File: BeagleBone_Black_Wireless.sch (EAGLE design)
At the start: 274 parts, among them IC1 OSD3358, IC10 TXS0108ERGYR, IC11 TXS0108ERGYR, IC12 TPS2051BDGN, IC13 SN74AUC1G74, IC14 TPD4S012DRY, IC15 TPD4S012DRY, IC17 SN74LVC2G241DCUR, IC18 TL1963ADCQR, IC19 AP2112K-1.8TRG1 3.3V, IC2 SN74LVC1G07DCK, IC3 SN74LVC1G06DCK, IC4 24LC32AT-I/OT, IC5 TLVH431 (SOT-23-3), IC6 DNP TLVH431 (SOT-23-3), IC7 IP4283CZ10-TBR, IC8 IP4283CZ10-TBR, Q2 32.768kHz, Q4 24 MHz, T1 MMBT2907, T2 DNP MMBT2907, T3 BSS138W-7-F, T4 BSS138W-7-F, X2 SCHA5B0200, X4 10118192-0001LF, X5 10118241-001RLF

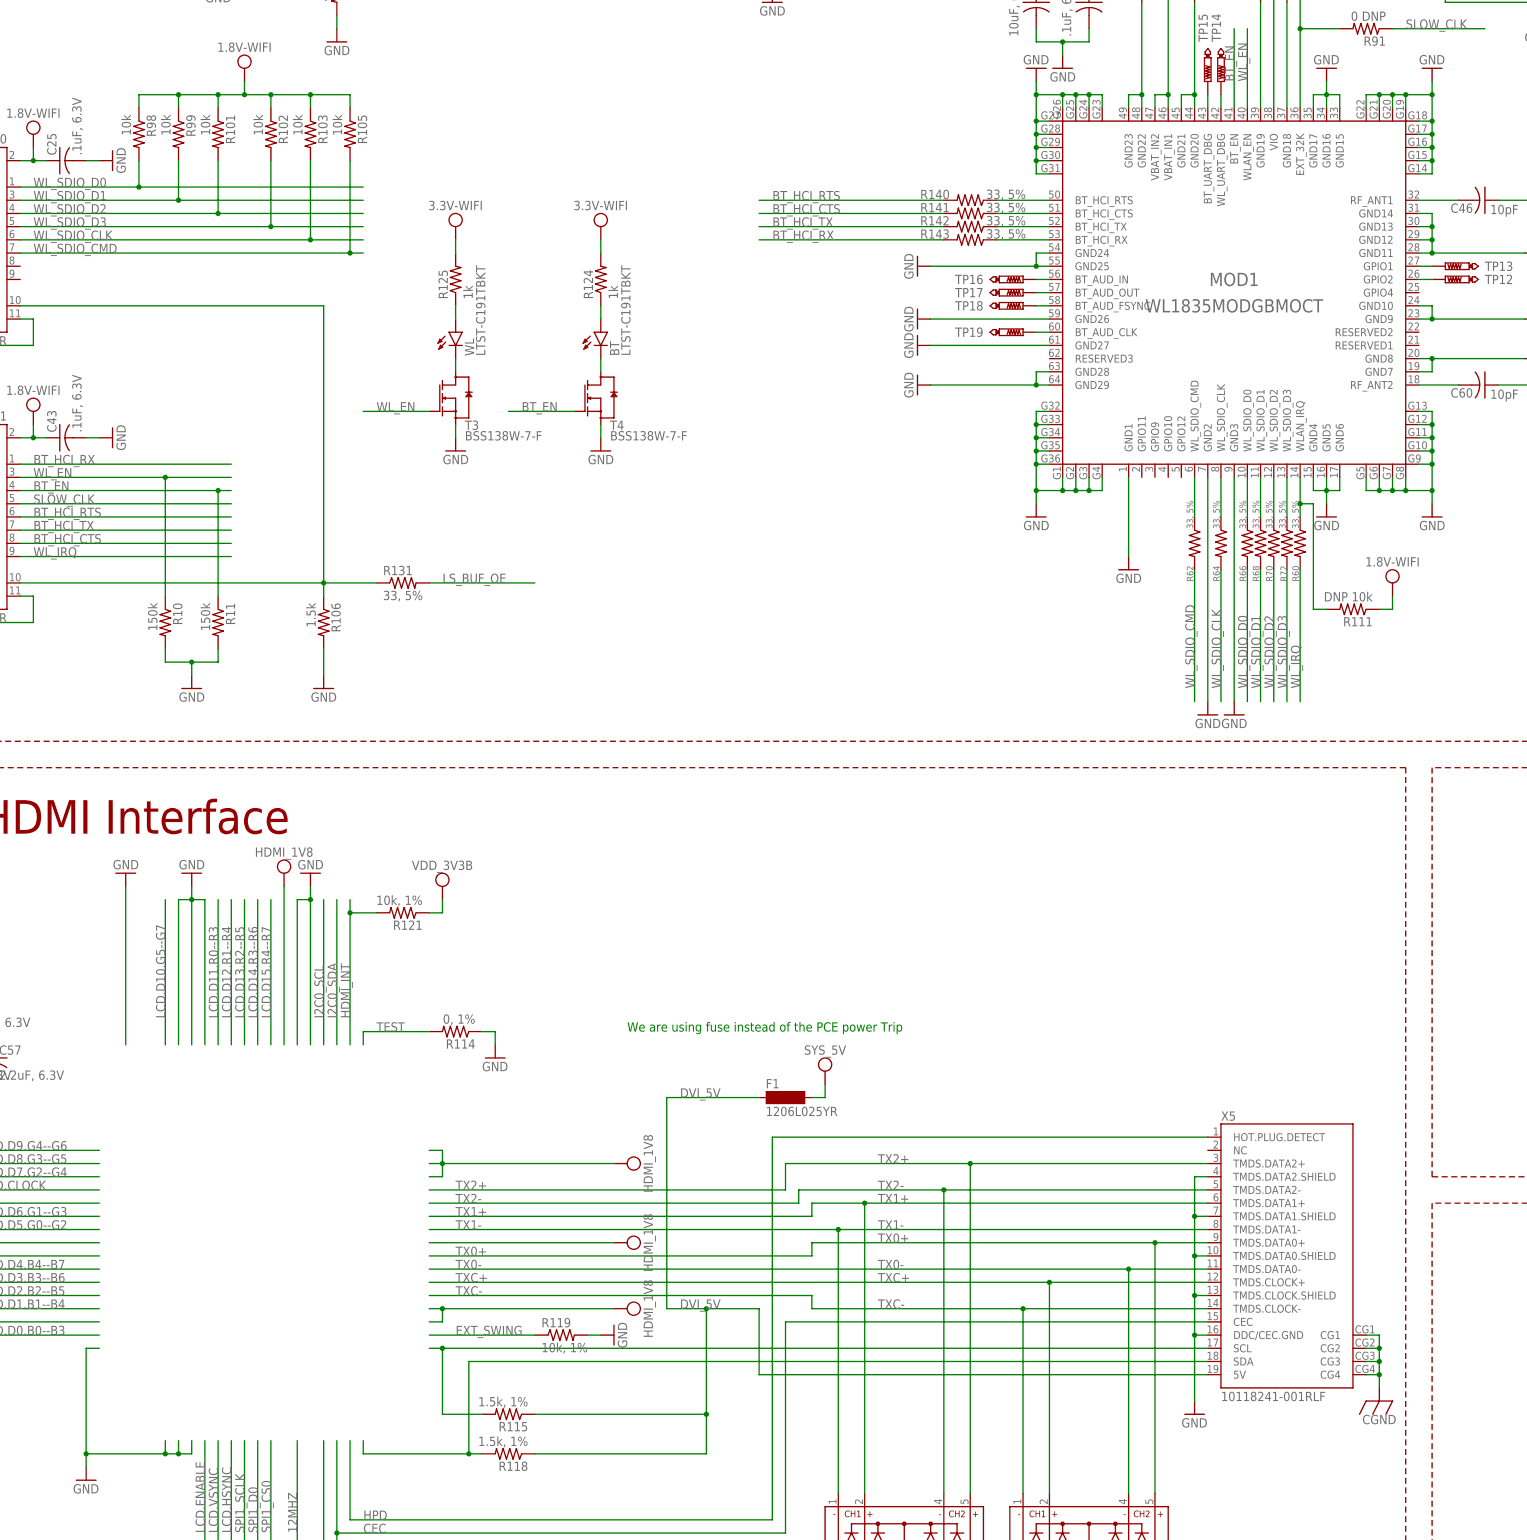
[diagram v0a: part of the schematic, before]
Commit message: removed MOD1 - added IC9 - adjusted routes
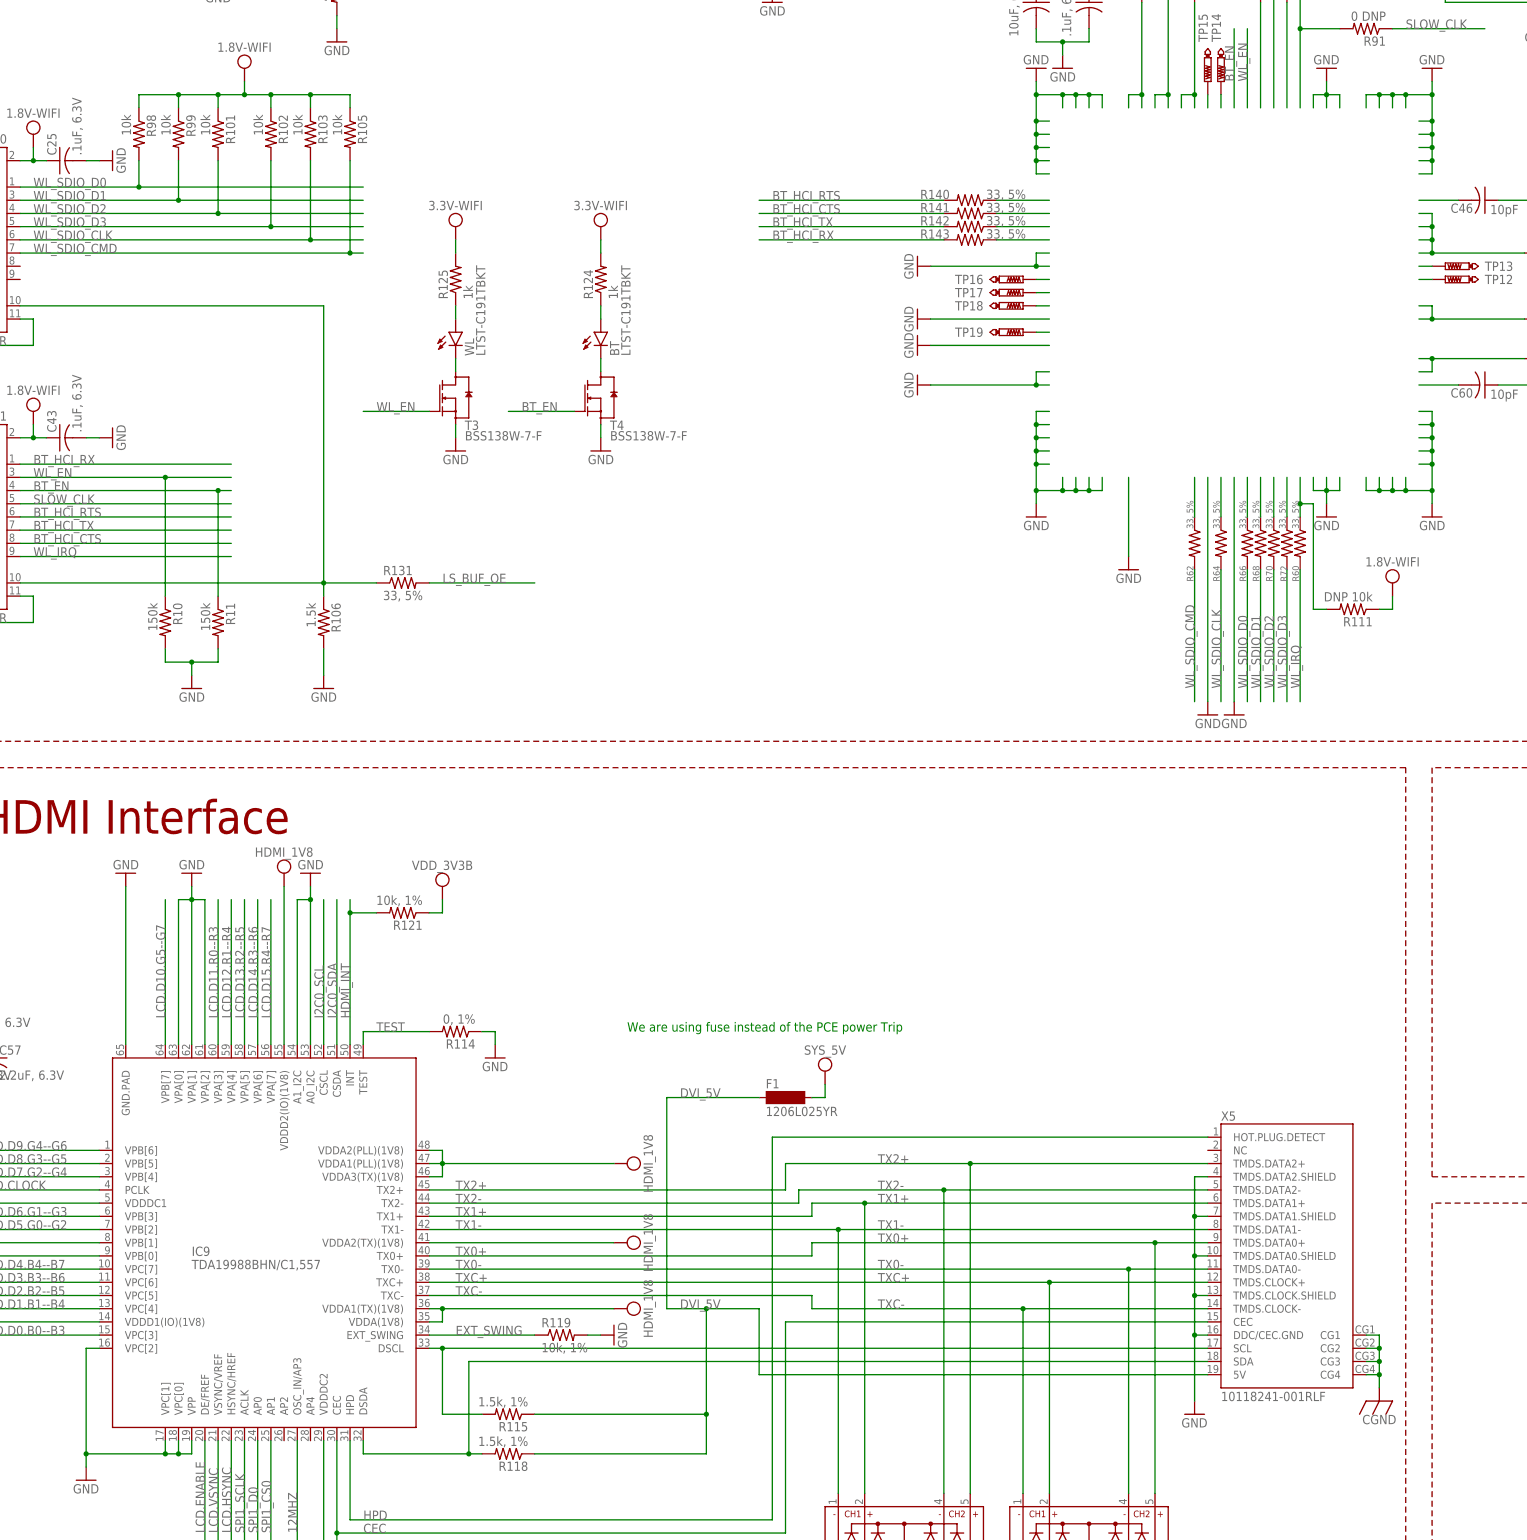
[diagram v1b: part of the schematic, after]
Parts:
- removed MOD1: WL1835MODGBMOCT, GHI-IC:WL1835MOD
- added IC9: TDA19988BHN/C1,557, GHI-IC:TDA19988BHN/C1
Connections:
- net 1.8V-WIFI: no longer MOD1.VIO
- net 12MHZ: now also IC9.OSC_IN/AP3
- net 3.3V-WIFI: no longer MOD1.VBAT_IN1, MOD1.VBAT_IN2
- net 32.768KHZ: no longer MOD1.EXT_32K
- net BT_EN: no longer MOD1.BT_EN
- net CEC: now also IC9.CEC
- net EXT_SWING: now also IC9.EXT_SWING
- net GND: now also IC9.A0_I2C, IC9.A1_I2C, IC9.GND.PAD, IC9.VPA[0], IC9.VPA[1], IC9.VPA[2], IC9.VPB[0], IC9.VPB[1], IC9.VPC[0], IC9.VPC[1], IC9.VPC[2], IC9.VPP; no longer MOD1.G1, MOD1.G10, MOD1.G11, MOD1.G12, MOD1.G13, MOD1.G14, MOD1.G15, MOD1.G16, MOD1.G17, MOD1.G18, MOD1.G19, MOD1.G2, MOD1.G20, MOD1.G21, MOD1.G22, MOD1.G23, MOD1.G24, MOD1.G25, MOD1.G26, MOD1.G27, MOD1.G28, MOD1.G29, MOD1.G3, MOD1.G30, MOD1.G31, MOD1.G32, MOD1.G33, MOD1.G34, MOD1.G35, MOD1.G36, MOD1.G4, MOD1.G5, MOD1.G6, MOD1.G7, MOD1.G8, MOD1.G9, MOD1.GND1, MOD1.GND10, MOD1.GND11, MOD1.GND12, MOD1.GND13, MOD1.GND14, MOD1.GND15, MOD1.GND16, MOD1.GND17, MOD1.GND18, MOD1.GND19, MOD1.GND2, MOD1.GND20, MOD1.GND21, MOD1.GND22, MOD1.GND23, MOD1.GND24, MOD1.GND25, MOD1.GND26, MOD1.GND27, MOD1.GND28, MOD1.GND29, MOD1.GND3, MOD1.GND4, MOD1.GND5, MOD1.GND6, MOD1.GND7, MOD1.GND8, MOD1.GND9
- net HDMI.DSCL: now also IC9.DSCL
- net HDMI.DSDA: now also IC9.DSDA
- net HDMI_1V8: now also IC9.VDDA(1V8), IC9.VDDA1(PLL)(1V8), IC9.VDDA1(TX)(1V8), IC9.VDDA2(PLL)(1V8), IC9.VDDA2(TX)(1V8), IC9.VDDA3(TX)(1V8), IC9.VDDD1(IO)(1V8), IC9.VDDD2(IO)(1V8), IC9.VDDDC1, IC9.VDDDC2
- net HDMI_INT: now also IC9.INT
- net HPD: now also IC9.HPD
- net I2C0_SCL: now also IC9.CSCL
- net I2C0_SDA: now also IC9.CSDA
- net LCD.CLOCK: now also IC9.PCLK
- net LCD.D0.B0--B3: now also IC9.VPC[3]
- net LCD.D1.B1--B4: now also IC9.VPC[4]
- net LCD.D10.G5--G7: now also IC9.VPB[7]
- net LCD.D11.R0--R3: now also IC9.VPA[3]
- net LCD.D12.R1--R4: now also IC9.VPA[4]
- net LCD.D13.R2--R5: now also IC9.VPA[5]
- net LCD.D14.R3--R6: now also IC9.VPA[6]
- net LCD.D15.R4--R7: now also IC9.VPA[7]
- net LCD.D2.B2--B5: now also IC9.VPC[5]
- net LCD.D3.B3--B6: now also IC9.VPC[6]
- net LCD.D4.B4--B7: now also IC9.VPC[7]
- net LCD.D5.G0--G2: now also IC9.VPB[2]
- net LCD.D6.G1--G3: now also IC9.VPB[3]
- net LCD.D7.G2--G4: now also IC9.VPB[4]
- net LCD.D8.G3--G5: now also IC9.VPB[5]
- net LCD.D9.G4--G6: now also IC9.VPB[6]
- net LCD.ENABLE: now also IC9.DE/FREF
- net LCD.HSYNC: now also IC9.HSYNC/HREF
- net LCD.VSYNC: now also IC9.VSYNC/VREF
- net N$15: no longer MOD1.RF_ANT1
- net N$19: no longer MOD1.RF_ANT2
- net N$33: no longer MOD1.GPIO2
- net N$35: no longer MOD1.GPIO1
- net N$38: no longer MOD1.WL_UART_DBG
- net N$39: no longer MOD1.BT_UART_DBG
- net N$40: no longer MOD1.BT_AUD_IN
- net N$41: no longer MOD1.BT_AUD_OUT
- net N$43: no longer MOD1.BT_AUD_FSYNC
- net N$44: no longer MOD1.BT_AUD_CLK
- net N$62: no longer MOD1.WLAN_IRQ
- net N$63: no longer MOD1.WL_SDIO_D3
- net N$64: no longer MOD1.WL_SDIO_D2
- net N$65: no longer MOD1.WL_SDIO_D1
- net N$67: no longer MOD1.WL_SDIO_D0
- net N$69: no longer MOD1.WL_SDIO_CLK
- net N$70: no longer MOD1.WL_SDIO_CMD
- net N$93: no longer MOD1.BT_HCI_RTS
- net N$94: no longer MOD1.BT_HCI_CTS
- net N$95: no longer MOD1.BT_HCI_TX
- net N$96: no longer MOD1.BT_HCI_RX
- net SPI1_CS0: now also IC9.AP1
- net SPI1_D0: now also IC9.AP0
- net SPI1_SCLK: now also IC9.ACLK
- net TEST: now also IC9.TEST
- net TX0+: now also IC9.TX0+
- net TX0-: now also IC9.TX0-
- net TX1+: now also IC9.TX1+
- net TX1-: now also IC9.TX1-
- net TX2+: now also IC9.TX2+
- net TX2-: now also IC9.TX2-
- net TXC+: now also IC9.TXC+
- net TXC-: now also IC9.TXC-
- net WL_EN: no longer MOD1.WLAN_EN
